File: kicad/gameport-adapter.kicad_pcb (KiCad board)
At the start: 2 copper layers, 45.7 x 39.4 mm, 8 parts, among them SW1 SW_DIP_x04, U1 Arduino_Pro_Micro

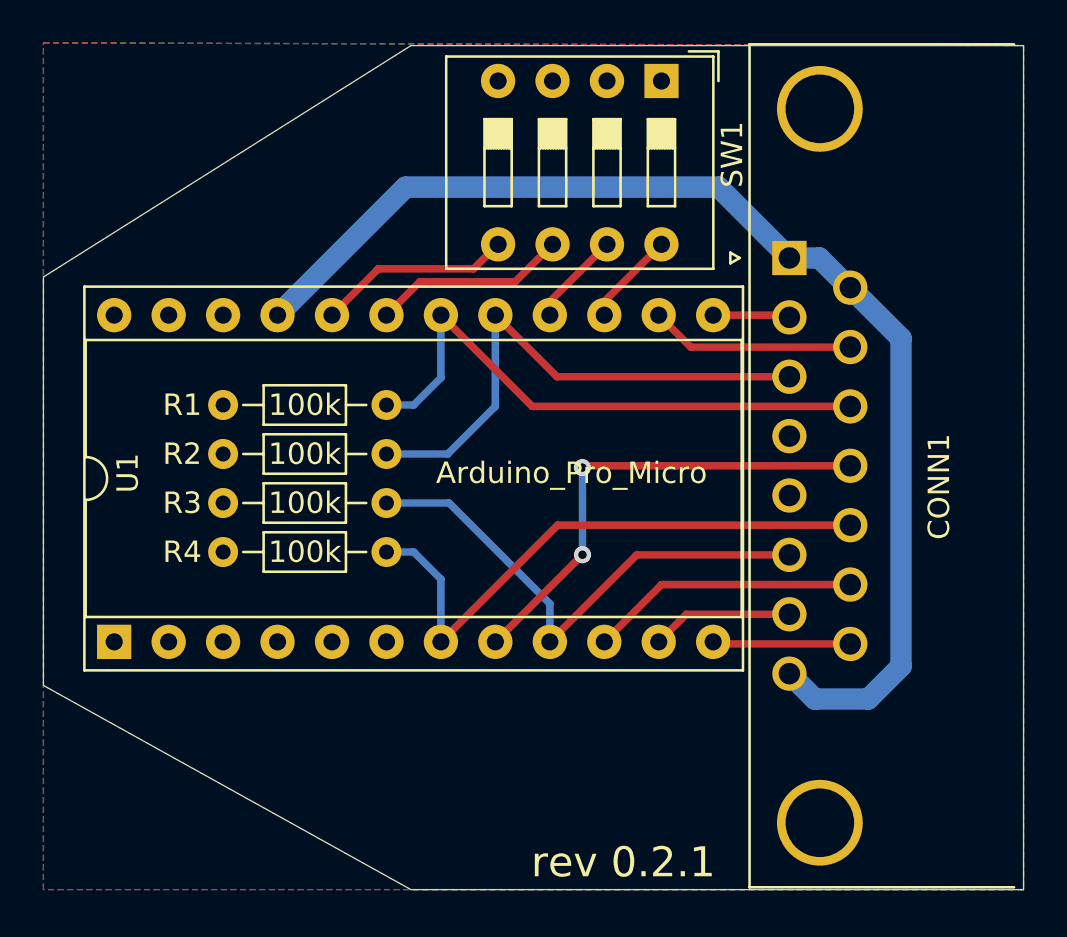
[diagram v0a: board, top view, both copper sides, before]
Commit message: Change the powersupply of the gameport to VIN/RAW rather than VCC
In my case with the Sidewinder 3D Pro the joystick did not seem
to run stable. Maybe there was too much power drawn from VCC?
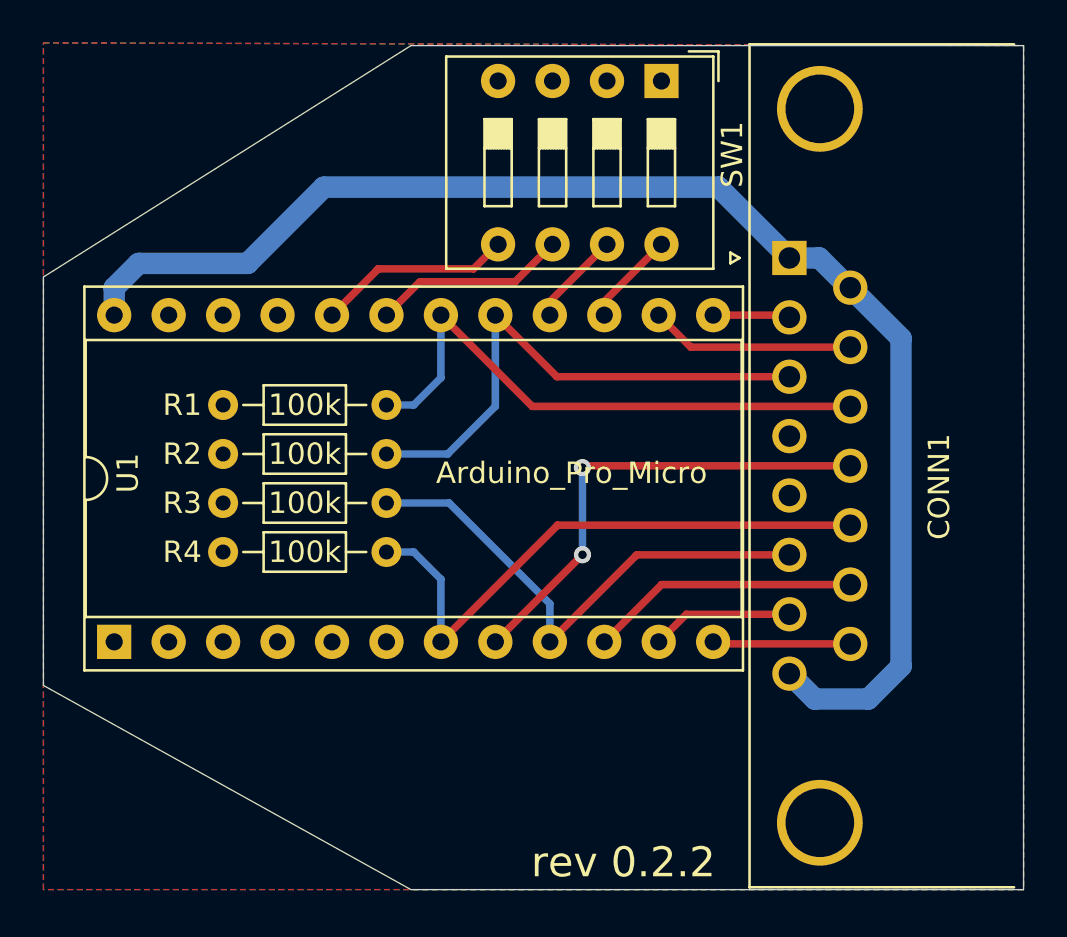
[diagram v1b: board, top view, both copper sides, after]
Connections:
- U1 pad 1: (no net) -> unconnected-(U1-Pad1)
- U1 pad 2: (no net) -> unconnected-(U1-Pad2)
- U1 pad 21: VCC -> unconnected-(U1-Pad21)
- U1 pad 22: (no net) -> unconnected-(U1-Pad22)
- U1 pad 24: (no net) -> VCC
- U1 pad 5: (no net) -> unconnected-(U1-Pad5)
- U1 pad 6: (no net) -> unconnected-(U1-Pad6)
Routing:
- net VCC: track 56.1 -> 64.5 mm
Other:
- board text added: "rev 0.2.2"
- board text removed: "rev 0.2.1"
